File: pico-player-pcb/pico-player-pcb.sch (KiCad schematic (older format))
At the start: 23 parts, among them J1 AudioPlug3, U1 Pico, U2 SN76489, U3 SN76489

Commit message: I think probably the pot was wired backward
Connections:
- net GND: now also RV1.3, RV1.6; no longer RV1.1, RV1.4
- net at C1.2: now also RV1.1; no longer RV1.3
- net at C2.2: now also RV1.4; no longer RV1.6
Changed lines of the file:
@@
 L power:GND #PWR012
 U 1 1 6041B584
-P 7950 3150
-F 0 "#PWR012" H 7950 2900 50  0001 C CNN
-F 1 "GND" H 7955 2977 50  0000 C CNN
-F 2 "" H 7950 3150 50  0001 C CNN
-F 3 "" H 7950 3150 50  0001 C CNN
-	1    7950 3150
+P 8250 3150
+F 0 "#PWR012" H 8250 2900 50  0001 C CNN
+F 1 "GND" H 8255 2977 50  0000 C CNN
+F 2 "" H 8250 3150 50  0001 C CNN
+F 3 "" H 8250 3150 50  0001 C CNN
+	1    8250 3150
 	1    0    0    -1
 $EndComp
@@
 Wire Wire Line
 	7850 2950 8100 2950
-Wire Wire Line
-	6850 3450 7800 3450
-Wire Wire Line
-	7800 3450 7800 3150
-Wire Wire Line
-	7800 3150 7750 3150
-Wire Wire Line
-	8400 3450 8300 3450
-Wire Wire Line
-	8300 3450 8300 3150
-Wire Wire Line
-	8300 3150 8250 3150
 $Comp
-L power:GND #PWR?
+L power:GND #PWR0101
 U 1 1 603DA506
-P 7450 3150
-F 0 "#PWR?" H 7450 2900 50  0001 C CNN
-F 1 "GND" H 7455 2977 50  0000 C CNN
-F 2 "" H 7450 3150 50  0001 C CNN
-F 3 "" H 7450 3150 50  0001 C CNN
-	1    7450 3150
+P 7750 3150
+F 0 "#PWR0101" H 7750 2900 50  0001 C CNN
+F 1 "GND" H 7755 2977 50  0000 C CNN
+F 2 "" H 7750 3150 50  0001 C CNN
+F 3 "" H 7750 3150 50  0001 C CNN
+	1    7750 3150
 	1    0    0    -1
 $EndComp
+Wire Wire Line
+	6850 3450 7250 3450
+Wire Wire Line
+	7250 3450 7250 3150
+Wire Wire Line
+	7250 3150 7450 3150
+Wire Wire Line
+	7900 3450 7900 3150
+Wire Wire Line
+	7900 3150 7950 3150
+Wire Wire Line
+	7900 3450 8400 3450
 $EndSCHEMATC

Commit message: ... sigh, it was better before
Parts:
- renumbered D1 to LED1, D2 to LED2, D3 to LED3, D4 to LED4, D5 to LED5, D6 to LED6, D7 to LED7, D8 to LED8
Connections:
- net GND: now also RV1.1, RV1.4; no longer RV1.3, RV1.6
- net d0: now reaches U1.1 (GPIO0), U2.10 (D0), U3.10 (D0)
- net d7: now reaches U1.10 (GPIO7), U2.3 (D7), U3.3 (D7)
- net we-1: now reaches U1.11 (GPIO8), U2.5 (~WE)
- net we-2: now reaches U1.12 (GPIO9), U3.5 (~WE)
- net oe-1: now reaches U1.14 (GPIO10), U2.6 (~OE)
- net oe-2: now reaches U1.15 (GPIO11), U3.6 (~OE)
- net clock: now reaches U1.16 (GPIO12), U2.14 (CLOCK), U3.14 (CLOCK)
- net d1: now reaches U1.2 (GPIO1), U2.11 (D1), U3.11 (D1)
- net led8: now reaches LED8.2 (A), U1.20 (GPIO15)
- net led7: now reaches LED7.2 (A), U1.21 (GPIO16)
- net led6: now reaches LED6.2 (A), U1.22 (GPIO17)
- net led5: now reaches LED5.2 (A), U1.24 (GPIO18)
- net led4: now reaches LED4.2 (A), U1.25 (GPIO19)
- net led3: now reaches LED3.2 (A), U1.26 (GPIO20)
- net led2: now reaches LED2.2 (A), U1.27 (GPIO21)
- net led1: now reaches LED1.2 (A), U1.29 (GPIO22)
- net d2: now reaches U1.4 (GPIO2), U2.12 (D2), U3.12 (D2)
- net d3: now reaches U1.5 (GPIO3), U2.13 (D3), U3.13 (D3)
- net d4: now reaches U1.6 (GPIO4), U2.15 (D4), U3.15 (D4)
- net d5: now reaches U1.7 (GPIO5), U2.1 (D5), U3.1 (D5)
- net d6: now reaches U1.9 (GPIO6), U2.2 (D6), U3.2 (D6)
- net at C1.2: now also RV1.3; no longer RV1.1
- net at C2.2: now also RV1.6; no longer RV1.4
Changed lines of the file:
@@
 $EndComp
 $Comp
-L Device:LED D8
+L Device:LED LED8
 U 1 1 602BBEAB
 P 5250 2650
-F 0 "D8" V 5197 2730 50  0000 L CNN
+F 0 "LED8" V 5197 2730 50  0000 L CNN
 F 1 "LED" V 5288 2730 50  0000 L CNN
 F 2 "LED_THT:LED_D5.0mm_Clear" H 5250 2650 50  0001 C CNN
@@
 $EndComp
 $Comp
-L Device:LED D1
+L Device:LED LED1
 U 1 1 602BC3E8
 P 3050 2650
-F 0 "D1" V 2997 2730 50  0000 L CNN
+F 0 "LED1" V 2997 2730 50  0000 L CNN
 F 1 "LED" V 3088 2730 50  0000 L CNN
 F 2 "LED_THT:LED_D5.0mm_Clear" H 3050 2650 50  0001 C CNN
@@
 $EndComp
 $Comp
-L Device:LED D2
+L Device:LED LED2
 U 1 1 602BCCD8
 P 3400 2650
-F 0 "D2" V 3347 2730 50  0000 L CNN
+F 0 "LED2" V 3347 2730 50  0000 L CNN
 F 1 "LED" V 3438 2730 50  0000 L CNN
 F 2 "LED_THT:LED_D5.0mm_Clear" H 3400 2650 50  0001 C CNN
@@
 $EndComp
 $Comp
-L Device:LED D3
+L Device:LED LED3
 U 1 1 602BCF86
 P 3750 2650
-F 0 "D3" V 3697 2730 50  0000 L CNN
+F 0 "LED3" V 3697 2730 50  0000 L CNN
 F 1 "LED" V 3788 2730 50  0000 L CNN
 F 2 "LED_THT:LED_D5.0mm_Clear" H 3750 2650 50  0001 C CNN
@@
 $EndComp
 $Comp
-L Device:LED D4
+L Device:LED LED4
 U 1 1 602BD44F
 P 4050 2650
-F 0 "D4" V 3997 2730 50  0000 L CNN
+F 0 "LED4" V 3997 2730 50  0000 L CNN
 F 1 "LED" V 4088 2730 50  0000 L CNN
 F 2 "LED_THT:LED_D5.0mm_Clear" H 4050 2650 50  0001 C CNN
@@
 $EndComp
 $Comp
-L Device:LED D5
+L Device:LED LED5
 U 1 1 602BD895
 P 4350 2650
-F 0 "D5" V 4297 2730 50  0000 L CNN
+F 0 "LED5" V 4297 2730 50  0000 L CNN
 F 1 "LED" V 4388 2730 50  0000 L CNN
 F 2 "LED_THT:LED_D5.0mm_Clear" H 4350 2650 50  0001 C CNN
@@
 $EndComp
 $Comp
-L Device:LED D6
+L Device:LED LED6
 U 1 1 602BDC3A
 P 4650 2650
-F 0 "D6" V 4597 2730 50  0000 L CNN
+F 0 "LED6" V 4597 2730 50  0000 L CNN
 F 1 "LED" V 4688 2730 50  0000 L CNN
 F 2 "LED_THT:LED_D5.0mm_Clear" H 4650 2650 50  0001 C CNN
@@
 $EndComp
 $Comp
-L Device:LED D7
+L Device:LED LED7
 U 1 1 602BE120
 P 4950 2650
-F 0 "D7" V 4897 2730 50  0000 L CNN
+F 0 "LED7" V 4897 2730 50  0000 L CNN
 F 1 "LED" V 4988 2730 50  0000 L CNN
 F 2 "LED_THT:LED_D5.0mm_Clear" H 4950 2650 50  0001 C CNN
@@
 L power:GND #PWR012
 U 1 1 6041B584
-P 8250 3150
-F 0 "#PWR012" H 8250 2900 50  0001 C CNN
-F 1 "GND" H 8255 2977 50  0000 C CNN
-F 2 "" H 8250 3150 50  0001 C CNN
-F 3 "" H 8250 3150 50  0001 C CNN
-	1    8250 3150
+P 7950 3150
+F 0 "#PWR012" H 7950 2900 50  0001 C CNN
+F 1 "GND" H 7955 2977 50  0000 C CNN
+F 2 "" H 7950 3150 50  0001 C CNN
+F 3 "" H 7950 3150 50  0001 C CNN
+	1    7950 3150
 	1    0    0    -1
 $EndComp
@@
 L power:GND #PWR0101
 U 1 1 603DA506
-P 7750 3150
-F 0 "#PWR0101" H 7750 2900 50  0001 C CNN
-F 1 "GND" H 7755 2977 50  0000 C CNN
-F 2 "" H 7750 3150 50  0001 C CNN
-F 3 "" H 7750 3150 50  0001 C CNN
-	1    7750 3150
-	1    0    0    -1
-$EndComp
-Wire Wire Line
-	6850 3450 7250 3450
-Wire Wire Line
-	7250 3450 7250 3150
-Wire Wire Line
-	7250 3150 7450 3150
-Wire Wire Line
-	7900 3450 7900 3150
-Wire Wire Line
-	7900 3150 7950 3150
-Wire Wire Line
-	7900 3450 8400 3450
+P 7450 3150
+F 0 "#PWR0101" H 7450 2900 50  0001 C CNN
+F 1 "GND" H 7455 2977 50  0000 C CNN
+F 2 "" H 7450 3150 50  0001 C CNN
+F 3 "" H 7450 3150 50  0001 C CNN
+	1    7450 3150
+	1    0    0    -1
+$EndComp
+Text Label 5050 3350 0    50   ~ 0
+led8
+Text Label 4750 3250 0    50   ~ 0
+led7
+Text Label 4450 3150 0    50   ~ 0
+led6
+Text Label 4150 3000 0    50   ~ 0
+led5
+Text Label 4000 2850 0    50   ~ 0
+led4
+Text Label 3750 2850 0    50   ~ 0
+led3
+Text Label 3400 3000 0    50   ~ 0
+led2
+Text Label 3050 3200 0    50   ~ 0
+led1
+Text Label 4900 5250 0    50   ~ 0
+d0
+Text Label 4900 5350 0    50   ~ 0
+d1
+Text Label 4900 5450 0    50   ~ 0
+d2
+Text Label 4900 5550 0    50   ~ 0
+d3
+Text Label 4900 5650 0    50   ~ 0
+d4
+Text Label 4900 5750 0    50   ~ 0
+d5
+Text Label 4900 5850 0    50   ~ 0
+d6
+Text Label 4900 5950 0    50   ~ 0
+d7
+Text Label 4900 6050 0    50   ~ 0
+we-1
+Text Label 4900 6150 0    50   ~ 0
+we-2
+Text Label 4900 6250 0    50   ~ 0
+oe-1
+Text Label 4900 6350 0    50   ~ 0
+oe-2
+Text Label 4900 6450 0    50   ~ 0
+clock
+Wire Wire Line
+	8250 3450 8250 3150
+Wire Wire Line
+	8250 3450 8400 3450
+Wire Wire Line
+	7750 3450 7750 3150
+Wire Wire Line
+	6850 3450 7750 3450
 $EndSCHEMATC

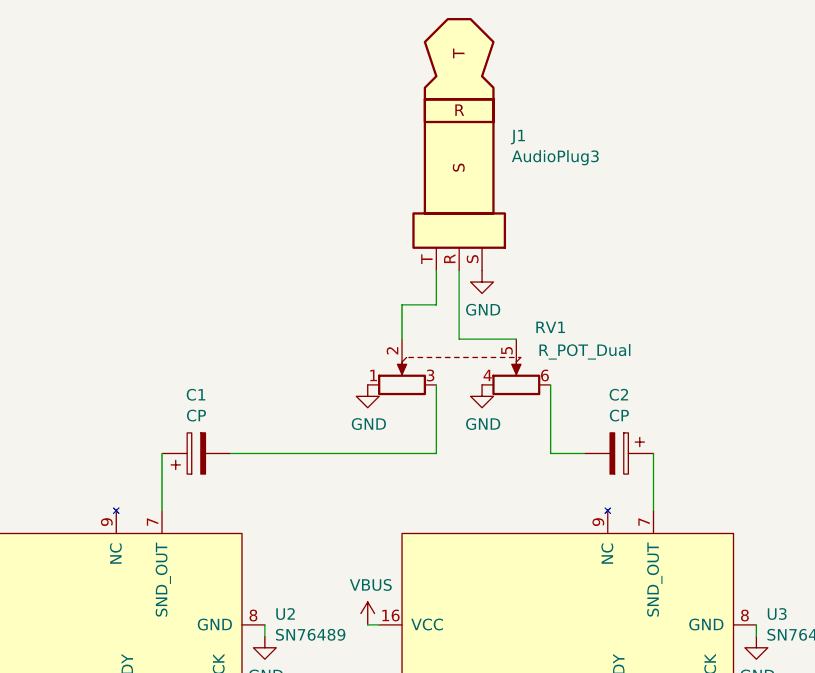
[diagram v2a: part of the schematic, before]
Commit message: rearrange slightly
the potentiometer was upside-down, at least when you install
a knob with a marker

it's nice to have the audio jack on the side, so you can
stand the board up
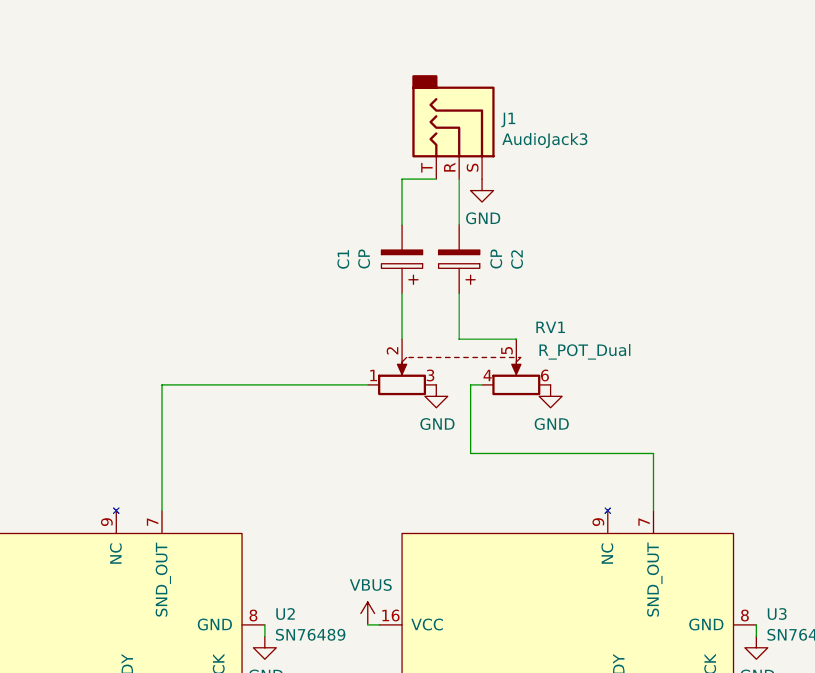
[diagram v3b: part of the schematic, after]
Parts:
- removed J1: AudioPlug3, Connector_Audio:Jack_3.5mm_CUI_SJ1-3533NG_Horizontal, symbol Connector:AudioPlug3
- added J1: AudioJack3, Connector_Audio:Jack_3.5mm_CUI_SJ1-3533NG_Horizontal, symbol Connector:AudioJack3
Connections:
- net GND: now also RV1.3, RV1.6, J1.S; no longer RV1.1, RV1.4
- net at U2.7 (SND_OUT): now also RV1.1; no longer C1.1
- net at U3.7 (SND_OUT): now also RV1.4; no longer C2.1
- net at C1.2: now also J1.T; no longer RV1.3
- net at C2.2: now also J1.R; no longer RV1.6
- net at RV1.2: now also C1.1
- net at RV1.5: now also C2.1
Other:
- moved on the sheet: C1, C2
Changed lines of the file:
@@
 L Device:CP C1
 U 1 1 603A8C73
-P 6700 3450
-F 0 "C1" V 6955 3450 50  0000 C CNN
-F 1 "CP" V 6864 3450 50  0000 C CNN
-F 2 "Capacitor_THT:CP_Radial_D5.0mm_P2.50mm" H 6738 3300 50  0001 C CNN
-F 3 "~" H 6700 3450 50  0001 C CNN
-	1    6700 3450
-	0    -1   -1   0
+P 7600 2600
+F 0 "C1" V 7855 2600 50  0000 C CNN
+F 1 "CP" V 7764 2600 50  0000 C CNN
+F 2 "Capacitor_THT:CP_Radial_D5.0mm_P2.50mm" H 7638 2450 50  0001 C CNN
+F 3 "~" H 7600 2600 50  0001 C CNN
+	1    7600 2600
+	-1   0    0    1
 $EndComp
 $Comp
 L Device:CP C2
 U 1 1 603AD0AE
-P 8550 3450
-F 0 "C2" V 8295 3450 50  0000 C CNN
-F 1 "CP" V 8386 3450 50  0000 C CNN
-F 2 "Capacitor_THT:CP_Radial_D5.0mm_P2.50mm" H 8588 3300 50  0001 C CNN
-F 3 "~" H 8550 3450 50  0001 C CNN
-	1    8550 3450
-	0    1    1    0
+P 7850 2600
+F 0 "C2" V 7595 2600 50  0000 C CNN
+F 1 "CP" V 7686 2600 50  0000 C CNN
+F 2 "Capacitor_THT:CP_Radial_D5.0mm_P2.50mm" H 7888 2450 50  0001 C CNN
+F 3 "~" H 7850 2600 50  0001 C CNN
+	1    7850 2600
+	-1   0    0    1
 $EndComp
-Wire Wire Line
-	6550 3700 6550 3450
 Wire Wire Line
 	8700 3450 8700 3700
@@
 L power:GND #PWR012
 U 1 1 6041B584
-P 7950 3150
-F 0 "#PWR012" H 7950 2900 50  0001 C CNN
-F 1 "GND" H 7955 2977 50  0000 C CNN
-F 2 "" H 7950 3150 50  0001 C CNN
-F 3 "" H 7950 3150 50  0001 C CNN
-	1    7950 3150
+P 8250 3150
+F 0 "#PWR012" H 8250 2900 50  0001 C CNN
+F 1 "GND" H 8255 2977 50  0000 C CNN
+F 2 "" H 8250 3150 50  0001 C CNN
+F 3 "" H 8250 3150 50  0001 C CNN
+	1    8250 3150
 	1    0    0    -1
-$EndComp
-$Comp
-L Connector:AudioPlug3 J1
-U 1 1 6042556D
-P 7850 2050
-F 0 "J1" V 7861 2280 50  0000 L CNN
-F 1 "AudioPlug3" V 7952 2280 50  0000 L CNN
-F 2 "Connector_Audio:Jack_3.5mm_CUI_SJ1-3533NG_Horizontal" H 7950 2000 50  0001 C CNN
-F 3 "~" H 7950 2000 50  0001 C CNN
-	1    7850 2050
-	0    1    1    0
 $EndComp
 $Comp
 L power:GND #PWR014
 U 1 1 6045E8DD
-P 7950 2650
-F 0 "#PWR014" H 7950 2400 50  0001 C CNN
-F 1 "GND" H 7955 2477 50  0000 C CNN
-F 2 "" H 7950 2650 50  0001 C CNN
-F 3 "" H 7950 2650 50  0001 C CNN
-	1    7950 2650
+P 7950 2250
+F 0 "#PWR014" H 7950 2000 50  0001 C CNN
+F 1 "GND" H 7955 2077 50  0000 C CNN
+F 2 "" H 7950 2250 50  0001 C CNN
+F 3 "" H 7950 2250 50  0001 C CNN
+	1    7950 2250
 	1    0    0    -1
 $EndComp
@@
 $EndComp
 Wire Wire Line
-	7600 2950 7600 2800
-Wire Wire Line
-	7600 2800 7750 2800
-Wire Wire Line
-	7750 2800 7750 2650
-Wire Wire Line
-	7850 2650 7850 2950
+	7850 2750 7850 2950
 Wire Wire Line
 	7850 2950 8100 2950
@@
 L power:GND #PWR0101
 U 1 1 603DA506
-P 7450 3150
-F 0 "#PWR0101" H 7450 2900 50  0001 C CNN
-F 1 "GND" H 7455 2977 50  0000 C CNN
-F 2 "" H 7450 3150 50  0001 C CNN
-F 3 "" H 7450 3150 50  0001 C CNN
-	1    7450 3150
+P 7750 3150
+F 0 "#PWR0101" H 7750 2900 50  0001 C CNN
+F 1 "GND" H 7755 2977 50  0000 C CNN
+F 2 "" H 7750 3150 50  0001 C CNN
+F 3 "" H 7750 3150 50  0001 C CNN
+	1    7750 3150
 	1    0    0    -1
 $EndComp
@@
 Text Label 4900 6450 0    50   ~ 0
 clock
+$Comp
+L Connector:AudioJack3 J1
+U 1 1 604C48C1
+P 7850 2050
+F 0 "J1" V 7786 2238 50  0000 L CNN
+F 1 "AudioJack3" V 7877 2238 50  0000 L CNN
+F 2 "Connector_Audio:Jack_3.5mm_CUI_SJ1-3533NG_Horizontal" H 7850 2050 50  0001 C CNN
+F 3 "~" H 7850 2050 50  0001 C CNN
+	1    7850 2050
+	0    1    1    0
+$EndComp
 Wire Wire Line
-	8250 3450 8250 3150
+	7900 3450 7900 3150
 Wire Wire Line
-	8250 3450 8400 3450
+	7900 3150 7950 3150
 Wire Wire Line
-	7750 3450 7750 3150
+	7600 2750 7600 2950
 Wire Wire Line
-	6850 3450 7750 3450
+	6550 3150 6550 3700
+Wire Wire Line
+	6550 3150 7450 3150
+Wire Wire Line
+	7900 3450 8700 3450
+Wire Wire Line
+	7850 2450 7850 2250
+Wire Wire Line
+	7600 2450 7600 2250
+Wire Wire Line
+	7600 2250 7750 2250
 $EndSCHEMATC
